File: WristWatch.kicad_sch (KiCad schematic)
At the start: 56 parts, among them J1 vcc, J2 gnd, J3 vcc, J4 gnd, Q1 Q_PMOS_GSD, Q2 Q_PMOS_GSD, U1 BQ51051BRHL, U2 STM32L412KBUx, U3 LIS2DE12, U4 AP2205-3.0, U5 MCP73832-2-OT, U6 ESP32-C3, Y1 32.768k, Y2 40M

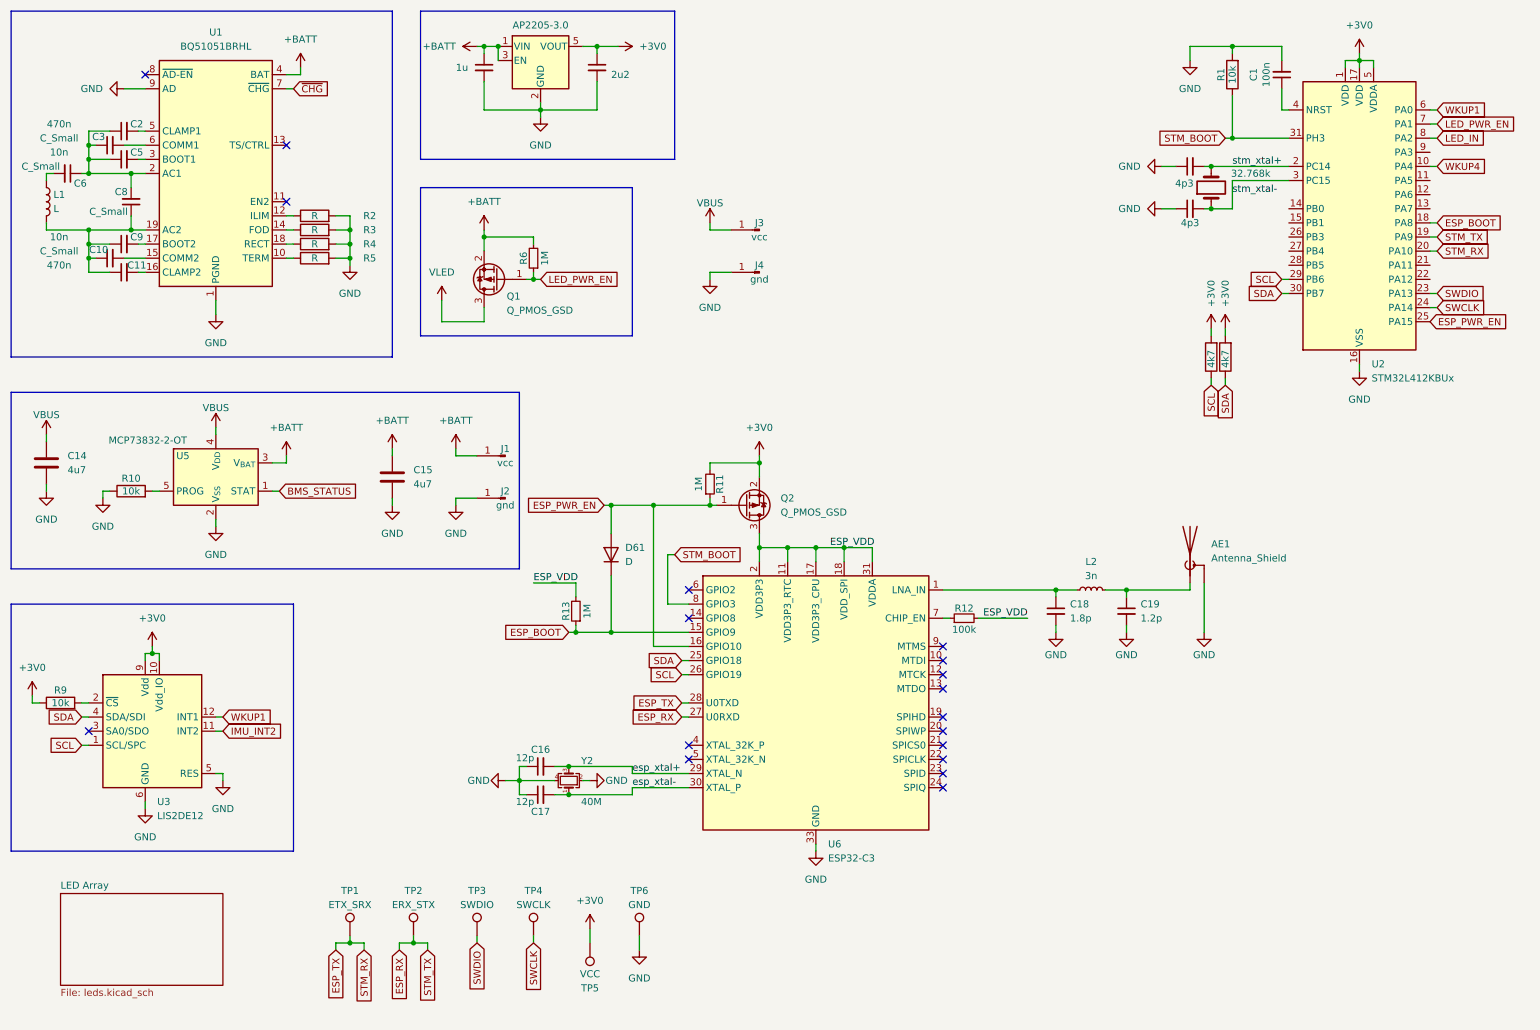
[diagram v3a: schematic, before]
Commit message: A much more reasonable architecture
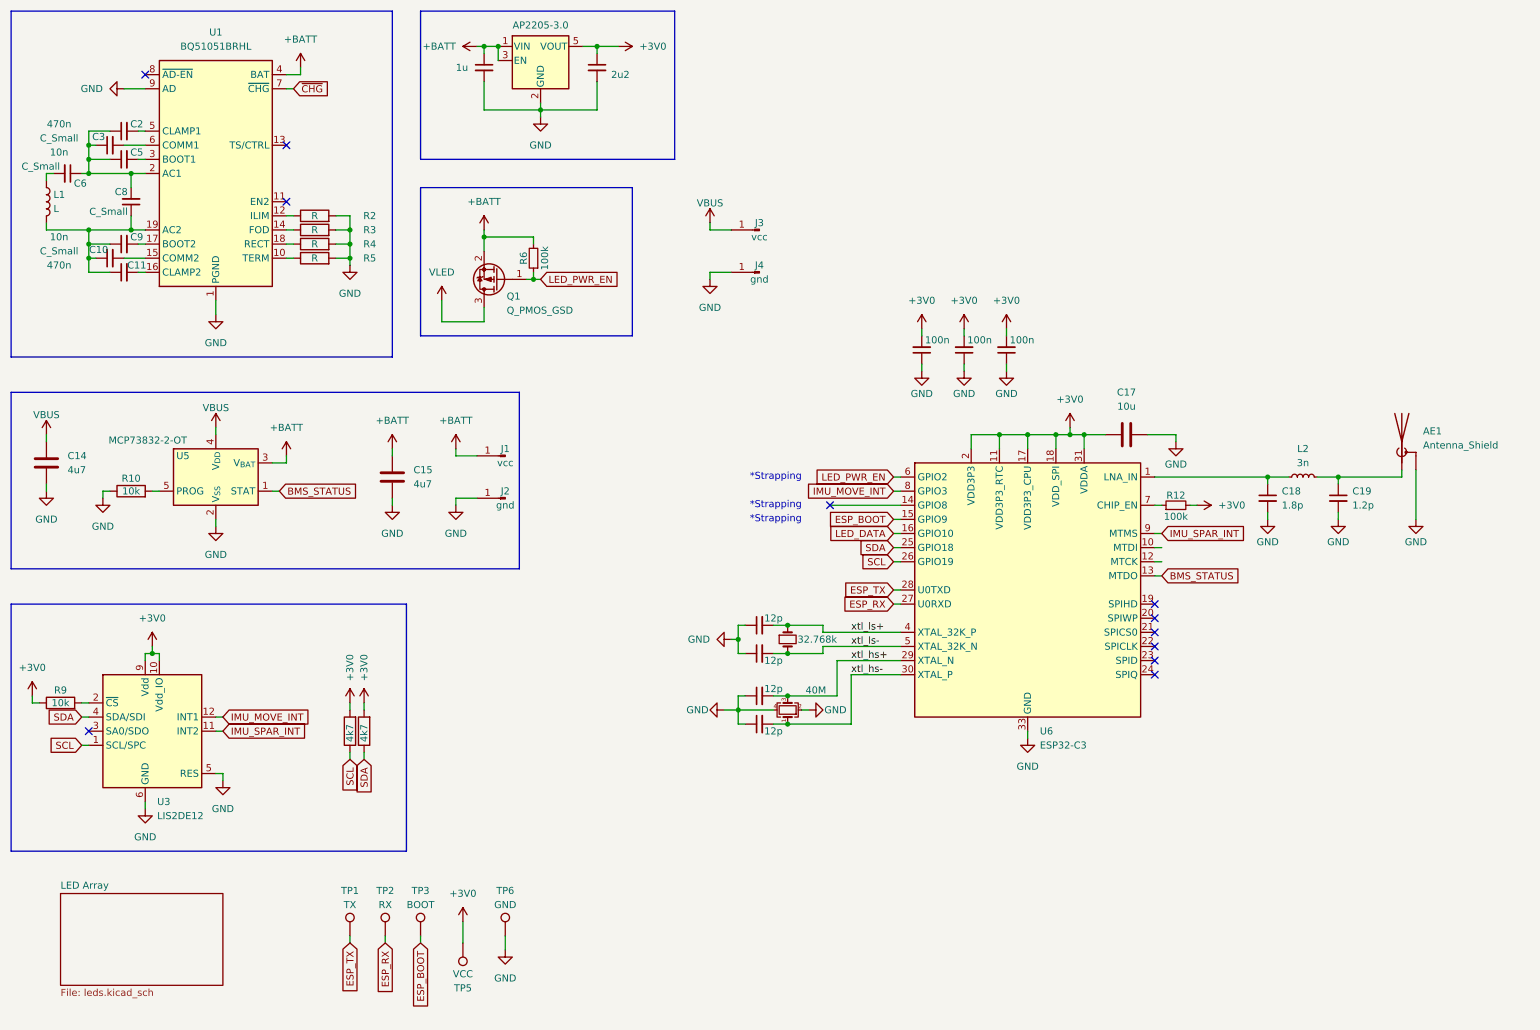
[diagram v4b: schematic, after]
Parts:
- removed C17: 12p, Capacitor_SMD:C_0402_1005Metric, symbol Device:C_Small
- removed D61: D, Diode_SMD:D_SOD-523, symbol Device:D
- removed Q2: Q_PMOS_GSD, Package_TO_SOT_SMD:SOT-523, symbol Device:Q_PMOS_GSD
- removed R1: 10k, Resistor_SMD:R_0402_1005Metric, symbol Device:R
- removed R11, R13: 1M, Resistor_SMD:R_0402_1005Metric, symbol Device:R_Small
- removed TP4: SWCLK, TestPoint:TestPoint_Pad_D1.5mm, symbol Connector:TestPoint
- removed U2: STM32L412KBUx, Package_DFN_QFN:QFN-32-1EP_5x5mm_P0.5mm_EP3.45x3.45mm, symbol MCU_ST_STM32L4:STM32L412KBUx
- removed Y1: 32.768k, Crystal:Crystal_SMD_3215-2Pin_3.2x1.5mm, symbol Device:Crystal
- added C17: 10u, symbol Device:C
- added C20, C21, C22: 100n, Capacitor_SMD:C_0402_1005Metric, symbol Device:C_Small
- added Y3: 32.768k, Crystal:Crystal_SMD_EuroQuartz_EQ161-2Pin_3.2x1.5mm, symbol Device:Crystal_Small
- C1: value 100n -> 12p; footprint Capacitor_SMD:C_0402_1005Metric -> (none)
- C16: footprint Capacitor_SMD:C_0402_1005Metric -> (none)
- C4, C7: value 4p3 -> 12p; footprint Capacitor_SMD:C_0402_1005Metric -> (none)
- R6: value 1M -> 100k
- TP1: value ETX_SRX -> TX
- TP2: value ERX_STX -> RX
- TP3: value SWDIO -> BOOT
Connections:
- net ESP_VDD is gone; now on net +3V0: R12.2, U6.11 (VDD3P3_RTC), U6.17 (VDD3P3_CPU), U6.18 (VDD_SPI), U6.2 (VDD3P3), U6.3 (VDD3P3), U6.31 (VDDA), U6.32 (VDDA)
- net IMU_INT2 is gone; now on net IMU_SPAR_INT: U3.11 (INT2)
- net SWDIO is gone; now on net ESP_BOOT: TP3.1
- net WKUP1 is gone; now on net IMU_MOVE_INT: U3.12 (INT1)
- net stm_xtal+ is gone; now on net xtl_ls-: C4.2
- net stm_xtal- is gone; now on net xtl_hs+: C7.2
- net +3V0: now also C17.1, C20.2, C21.2, C22.2
- net BMS_STATUS: now also U6.13 (MTDO)
- net GND: now also C1.1, C17.2, C20.1, C21.1, C22.1; no longer C1.2
- net LED_PWR_EN: now also U6.6 (GPIO2)
- net xtl_ls+: now reaches U6.4 (XTAL_32K_P)
- net xtl_ls+: now also C1.2, Y3.1
- net xtl_ls-: now reaches U6.5 (XTAL_32K_N)
- net xtl_ls-: now also Y3.2
- net IMU_SPAR_INT: now reaches U6.9 (MTMS)
- net ESP_PWR_EN renamed LED_DATA
- net STM_BOOT renamed IMU_MOVE_INT
- net esp_xtal+ renamed xtl_hs+
- net xtl_hs+: no longer C16.2
- net esp_xtal- renamed xtl_hs-
- net xtl_hs-: now also C16.2
- no-connect marks 18 -> 11
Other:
- note added: "*Strapping"
- moved on the sheet: AE1, C18, C19, L2, R12, TP2, TP5, TP6, U6
